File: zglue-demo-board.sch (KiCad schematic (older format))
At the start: 53 parts, among them J1 0473460001, J2 DF13A-2P-1.25H, J3 20021121-00010C4LF, J4 2x20_Header_Female, J5 0473460001, J6 556500488, J7 556500488, J8 WE_686115148922, J9 WE_686115148922, U1 FT232RQ-REEL, U2 NTB0104BQ, U3 NTB0104BQ, U4 NTB0104BQ

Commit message: Added FT4232
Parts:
- removed C4, C6: C_47p_0402, antmicro-footprints:0402-cap, symbol antmicroCapacitors0402:C_47p_0402
- removed C5, C7, C8: C_100n_0402_6V3, antmicro-footprints:0402-cap, symbol antmicroCapacitors0402:C_100n_0402_6V3
- removed D1: TPD2EUSB30DRTR, antmicro-footprints:SOT-3, symbol antmicroTVSDiodes:TPD2EUSB30DRTR
- removed J1: 0473460001, antmicro-footprints:USB_Micro_B_Female_0473460001, symbol antmicroUSBDVIHDMIConnectors:0473460001
- removed R2, R3: R_22R_0402, antmicro-footprints:0402-res, symbol antmicroResistors0402:R_22R_0402
- removed U1: FT232RQ-REEL, antmicro-footprints:QFN-32-1EP_5x5mm, symbol antmicroInterfaceControllers:FT232RQ-REEL
- added C15, C16, C17, C18, C19, C20, C21, C22, C23, C24, C?: C_100n_0402_6V3, antmicro-footprints:0402-cap, symbol antmicroCapacitors0402:C_100n_0402_6V3
- added C25, C26: C_4u7_0402, antmicro-footprints:0402-cap, symbol antmicroCapacitors0402:C_4u7_0402
- added C?: C_10u_0603, antmicro-footprints:0603-cap, symbol antmicroCapacitors0603:C_10u_0603
- added D5: TPD2EUSB30DRTR, antmicro-footprints:SOT-3, symbol antmicroTVSDiodes:TPD2EUSB30DRTR
- added FB1, FB2: BLM18AG601SN1D, antmicro-footprints:0603, symbol antmicroFerriteBeadsandChips:BLM18AG601SN1D
- added J10: 0473460001, antmicro-footprints:USB_Micro_B_Female_0473460001, symbol antmicroUSBDVIHDMIConnectors:0473460001
- added JP1, JP2, JP3: Jumper_3_Open, symbol Jumper:Jumper_3_Open
- added R10, R5: R_2k_0402, antmicro-footprints:0402-res, symbol antmicroResistors0402:R_2k_0402
- added R11, R12, R13, R14, R15, R16, R17, R18, R19, R2, R20, R21, R22, R23, R24, R25, R26, R27, R28, R29, R3, R30, R31, R32, R33, R8: R_0R_0402, antmicro-footprints:0402-res, symbol antmicroResistors0402:R_0R_0402
- added R4, R6, R7: R_10k_0402, antmicro-footprints:0402-res, symbol antmicroResistors0402:R_10k_0402
- added R9: R_12k_0402, antmicro-footprints:0402-res, symbol antmicroResistors0402:R_12k_0402
- added U5: 93LC56CT-IMC, antmicro-footprints:SOIC-8_W3.9mm, symbol antmicroMemory:93LC56CT-IMC
- added U6: FT4232HQ, antmicro-footprints:FT4232HQ, symbol antmicroInterfaceControllers:FT4232HQ
- added U?: LD1117S33CTR, antmicro-footprints:SOT-223, symbol antmicroPMICVoltageRegulatorsLinear:LD1117S33CTR
- added Y1: ASFLMB-12.000MHZ-LC-T, antmicro-footprints:ASFLMB, symbol antmicroOscillators:ASFLMB-12.000MHZ-LC-T
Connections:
- net labels added: 1V8_FTDI, 3V3_FTDI, CTRL_RST_FLASH_SOC_CS, FLASH_CLK, FLASH_CS, FLASH_IO0, FLASH_IO1, FLASH_IO2, FLASH_IO3, PROG_USB_D_N, PROG_USB_D_P, VCCIO, VCCIO1, VCCIO2, VCCIO3, VPHY, VPLL
- net labels removed: PIO1, PIO2, PIO3
- wire segments 281 -> 419
- no-connect marks 23 -> 27
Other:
- note added: "Flash Programming FTDI"
- note added: "Flash Programming USB connector"
- note added: "LDO for FTDI"
- note added: "TODO: no Done signal"
- note removed: "Debug FTDI"
- note removed: "Programming USB connector"
- moved on the sheet: C1, C10, C11, C12, C13, C14, C2, C3, C9, D2, D3, D4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

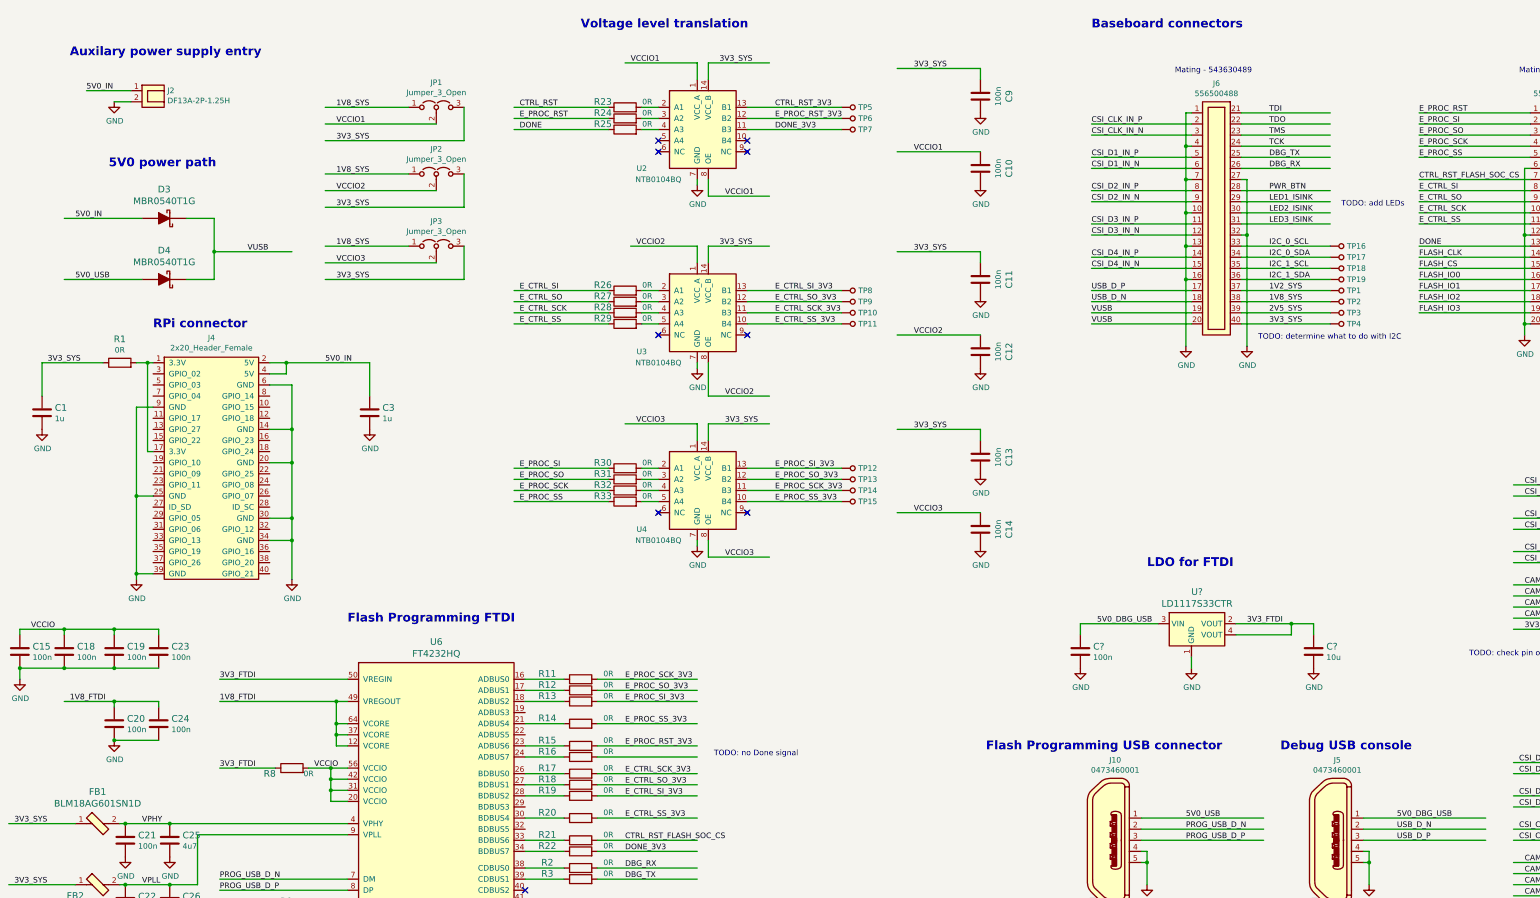
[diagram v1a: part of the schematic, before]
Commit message: Fixed power path
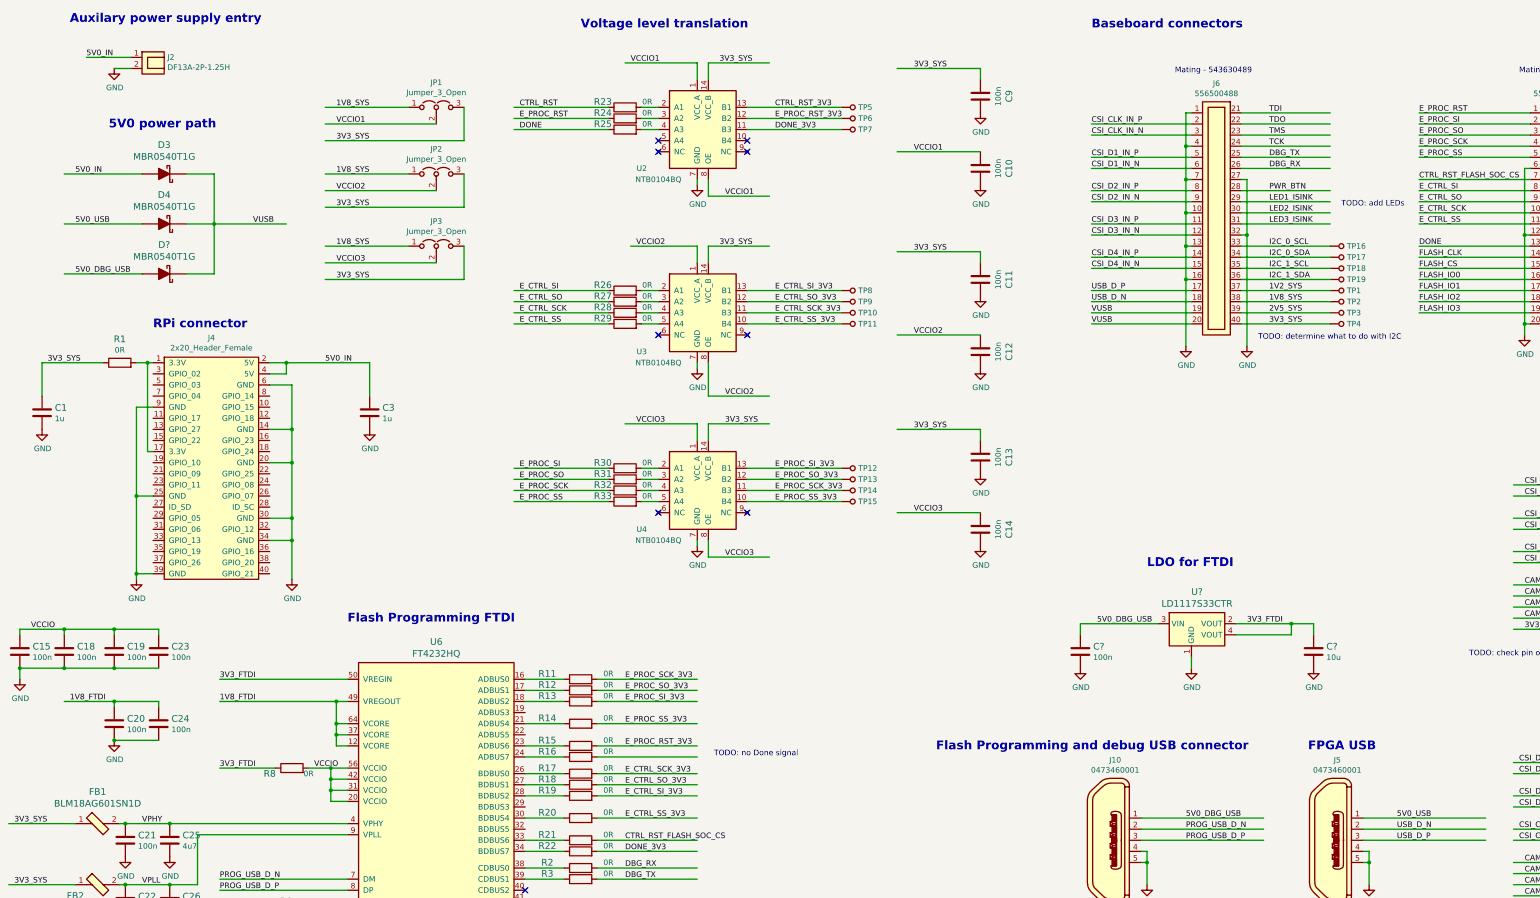
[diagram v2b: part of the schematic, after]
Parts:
- added D?: MBR0540T1G, antmicro-footprints:SOD-123, symbol antmicroDiodesRectifiersSingle:MBR0540T1G
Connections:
- wire segments 419 -> 421
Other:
- note added: "FPGA USB"
- note added: "Flash Programming and debug USB connector"
- note removed: "Debug USB console"
- note removed: "Flash Programming USB connector"
- moved on the sheet: D3, D4, J2
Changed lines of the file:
@@
 L antmicroDF13Connectors:DF13A-2P-1.25H J2
 U 1 1 5DA507A8
-P 1850 1550
-F 0 "J2" H 1978 1701 50  0000 L CNN
-F 1 "DF13A-2P-1.25H" H 1978 1610 50  0000 L CNN
-F 2 "antmicro-footprints:DF13A-2P-1.25H" H 1750 1100 50  0001 C CNN
-F 3 "" H 1850 1500 50  0001 C CNN
-F 4 "DF13A-2P-1.25H" H 1900 1300 50  0001 C CNN "MPN"
-F 5 "Hirose" H 1850 1200 50  0001 C CNN "Manufacturer"
-	1    1850 1550
+P 1850 1250
+F 0 "J2" H 1978 1401 50  0000 L CNN
+F 1 "DF13A-2P-1.25H" H 1978 1310 50  0000 L CNN
+F 2 "antmicro-footprints:DF13A-2P-1.25H" H 1750 800 50  0001 C CNN
+F 3 "" H 1850 1200 50  0001 C CNN
+F 4 "DF13A-2P-1.25H" H 1900 1000 50  0001 C CNN "MPN"
+F 5 "Hirose" H 1850 900 50  0001 C CNN "Manufacturer"
+	1    1850 1250
 	1    0    0    -1
 $EndComp
@@
 3V3_SYS
 Wire Wire Line
-	1650 1400 1250 1400
+	1650 1100 1250 1100
 $Comp
 L power:GND #PWR03
 U 1 1 5DA5701F
-P 1500 1500
-F 0 "#PWR03" H 1500 1250 50  0001 C CNN
-F 1 "GND" H 1505 1327 50  0000 C CNN
-F 2 "" H 1500 1500 50  0001 C CNN
-F 3 "" H 1500 1500 50  0001 C CNN
-	1    1500 1500
-	1    0    0    -1
-$EndComp
-Wire Wire Line
-	1650 1500 1500 1500
+P 1500 1200
+F 0 "#PWR03" H 1500 950 50  0001 C CNN
+F 1 "GND" H 1505 1027 50  0000 C CNN
+F 2 "" H 1500 1200 50  0001 C CNN
+F 3 "" H 1500 1200 50  0001 C CNN
+	1    1500 1200
+	1    0    0    -1
+$EndComp
+Wire Wire Line
+	1650 1200 1500 1200
 $Comp
 L antmicroRectangularConnectorsHeadersMalePins:20021121-00010C4LF J3
@@
 	7700 10500 7550 10500
 Connection ~ 7550 10500
-Text Label 1250 1400 0    50   ~ 0
+Text Label 1250 1100 0    50   ~ 0
 5V0_IN
 $Comp
@@
 	1    0    0    -1
 $EndComp
-Text Notes 1100 1100 0    79   ~ 16
+Text Notes 1100 800  0    79   ~ 16
 Auxilary power supply entry
 Text Notes 1850 3550 0    79   ~ 16
@@
 	1    0    0    -1
 $EndComp
-Text Label 13050 7950 0    50   ~ 0
+Text Label 11150 7950 0    50   ~ 0
 5V0_DBG_USB
 Text Label 3400 3850 0    50   ~ 0
@@
 	1    0    0    -1
 $EndComp
-Text Notes 12000 7350 0    79   ~ 16
-Debug USB console
+Text Notes 12250 7350 0    79   ~ 16
+FPGA USB
 $Comp
 L antmicroTestPoints:TP_SMD1MM TP1
@@
 L antmicroDiodesRectifiersSingle:MBR0540T1G D3
 U 1 1 5DD6DAC1
-P 1950 2550
-F 0 "D3" H 1950 2812 60  0000 C CNN
-F 1 "MBR0540T1G" H 1950 2706 60  0000 C CNN
-F 2 "antmicro-footprints:SOD-123" H 2150 2750 60  0001 L CNN
-F 3 "http://www.onsemi.com/pub/Collateral/MBR0540T1-D.PDF" H 2150 2850 60  0001 L CNN
-F 4 "MBR0540T1G" H 2150 3050 60  0001 L CNN "MPN"
-F 5 "ON Semiconductor" H 2150 3650 60  0001 L CNN "Manufacturer"
-	1    1950 2550
+P 1950 2150
+F 0 "D3" H 1950 2412 60  0000 C CNN
+F 1 "MBR0540T1G" H 1950 2306 60  0000 C CNN
+F 2 "antmicro-footprints:SOD-123" H 2150 2350 60  0001 L CNN
+F 3 "http://www.onsemi.com/pub/Collateral/MBR0540T1-D.PDF" H 2150 2450 60  0001 L CNN
+F 4 "MBR0540T1G" H 2150 2650 60  0001 L CNN "MPN"
+F 5 "ON Semiconductor" H 2150 3250 60  0001 L CNN "Manufacturer"
+	1    1950 2150
 	1    0    0    -1
 $EndComp
@@
 L antmicroDiodesRectifiersSingle:MBR0540T1G D4
 U 1 1 5DD6DCA3
-P 1950 3100
-F 0 "D4" H 1950 3362 60  0000 C CNN
-F 1 "MBR0540T1G" H 1950 3256 60  0000 C CNN
-F 2 "antmicro-footprints:SOD-123" H 2150 3300 60  0001 L CNN
-F 3 "http://www.onsemi.com/pub/Collateral/MBR0540T1-D.PDF" H 2150 3400 60  0001 L CNN
-F 4 "MBR0540T1G" H 2150 3600 60  0001 L CNN "MPN"
-F 5 "ON Semiconductor" H 2150 4200 60  0001 L CNN "Manufacturer"
-	1    1950 3100
-	1    0    0    -1
-$EndComp
-Wire Wire Line
-	1750 2550 1050 2550
-Wire Wire Line
-	1750 3100 1050 3100
-Wire Wire Line
-	2150 2550 2400 2550
-Wire Wire Line
-	2400 2550 2400 2850
-Wire Wire Line
-	2400 2850 3100 2850
-Wire Wire Line
-	2400 2850 2400 3100
-Wire Wire Line
-	2400 3100 2150 3100
-Connection ~ 2400 2850
-Text Label 2700 2850 0    50   ~ 0
+P 1950 2600
+F 0 "D4" H 1950 2862 60  0000 C CNN
+F 1 "MBR0540T1G" H 1950 2756 60  0000 C CNN
+F 2 "antmicro-footprints:SOD-123" H 2150 2800 60  0001 L CNN
+F 3 "http://www.onsemi.com/pub/Collateral/MBR0540T1-D.PDF" H 2150 2900 60  0001 L CNN
+F 4 "MBR0540T1G" H 2150 3100 60  0001 L CNN "MPN"
+F 5 "ON Semiconductor" H 2150 3700 60  0001 L CNN "Manufacturer"
+	1    1950 2600
+	1    0    0    -1
+$EndComp
+Wire Wire Line
+	1750 2150 1050 2150
+Wire Wire Line
+	1750 2600 1050 2600
+Wire Wire Line
+	2150 2150 2400 2150
+Wire Wire Line
+	2400 2600 2150 2600
+Text Label 2750 2600 0    50   ~ 0
 VUSB
-Text Label 1150 2550 0    50   ~ 0
+Text Label 1150 2150 0    50   ~ 0
 5V0_IN
-Text Label 1150 3100 0    50   ~ 0
+Text Label 1150 2600 0    50   ~ 0
 5V0_USB
-Text Notes 1450 2100 0    79   ~ 16
+Text Notes 1450 1750 0    79   ~ 16
 5V0 power path
 $Comp
@@
 	1    0    0    -1
 $EndComp
-Text Label 11150 7950 0    50   ~ 0
+Text Label 13050 7950 0    50   ~ 0
 5V0_USB
 Text Label 11150 8150 0    50   ~ 0
@@
 Text Label 11150 8050 0    50   ~ 0
 PROG_USB_D_N
-Text Notes 9350 7350 0    79   ~ 16
-Flash Programming USB connector
+Text Notes 8900 7350 0    79   ~ 16
+Flash Programming and debug USB connector
 $Comp
 L antmicroTVSDiodes:TPD2EUSB30DRTR D5
@@
 	12300 6200 12300 6300
 Connection ~ 12100 6200
+$Comp
+L antmicroDiodesRectifiersSingle:MBR0540T1G D?
+U 1 1 5DB10412
+P 1950 3050
+F 0 "D?" H 1950 3312 60  0000 C CNN
+F 1 "MBR0540T1G" H 1950 3206 60  0000 C CNN
+F 2 "antmicro-footprints:SOD-123" H 2150 3250 60  0001 L CNN
+F 3 "http://www.onsemi.com/pub/Collateral/MBR0540T1-D.PDF" H 2150 3350 60  0001 L CNN
+F 4 "MBR0540T1G" H 2150 3550 60  0001 L CNN "MPN"
+F 5 "ON Semiconductor" H 2150 4150 60  0001 L CNN "Manufacturer"
+	1    1950 3050
+	1    0    0    -1
+$EndComp
+Wire Wire Line
+	2400 2150 2400 2600
+Wire Wire Line
+	2400 2600 2400 3050
+Wire Wire Line
+	2400 3050 2150 3050
+Connection ~ 2400 2600
+Wire Wire Line
+	2400 2600 3050 2600
+Wire Wire Line
+	1750 3050 1050 3050
+Text Label 1150 3050 0    50   ~ 0
+5V0_DBG_USB
 $EndSCHEMATC

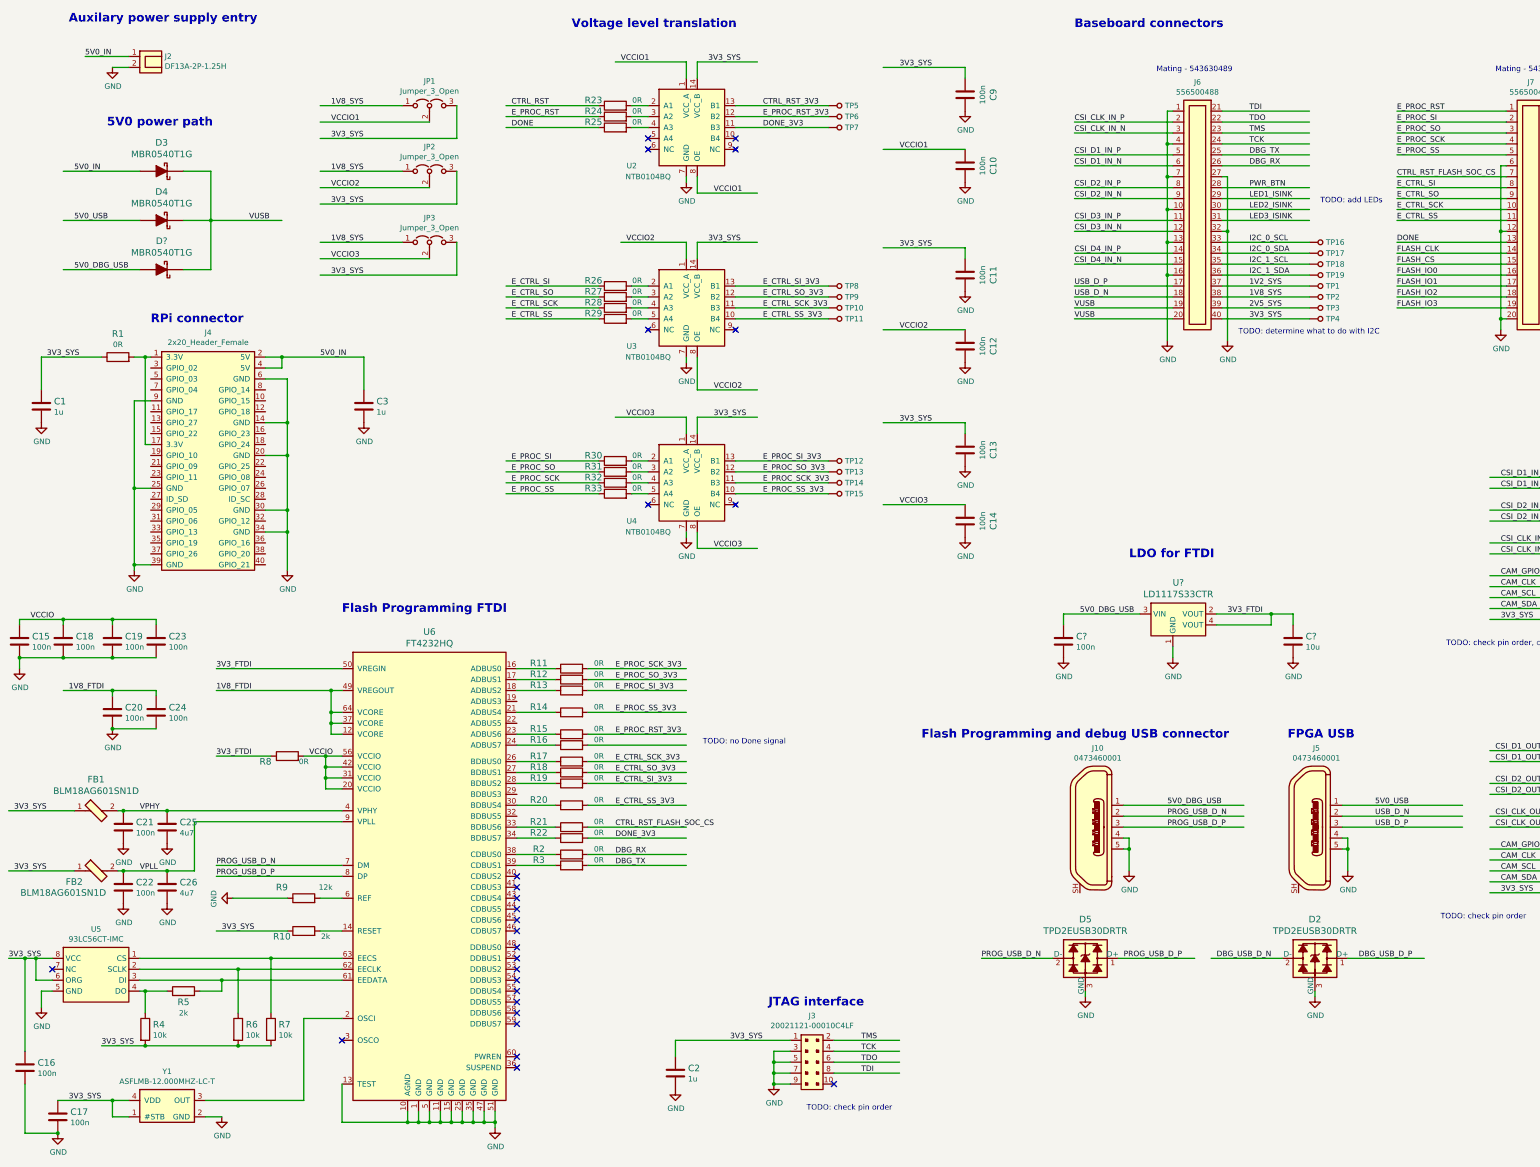
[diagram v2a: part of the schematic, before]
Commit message: Unified 3V3 voltage rails
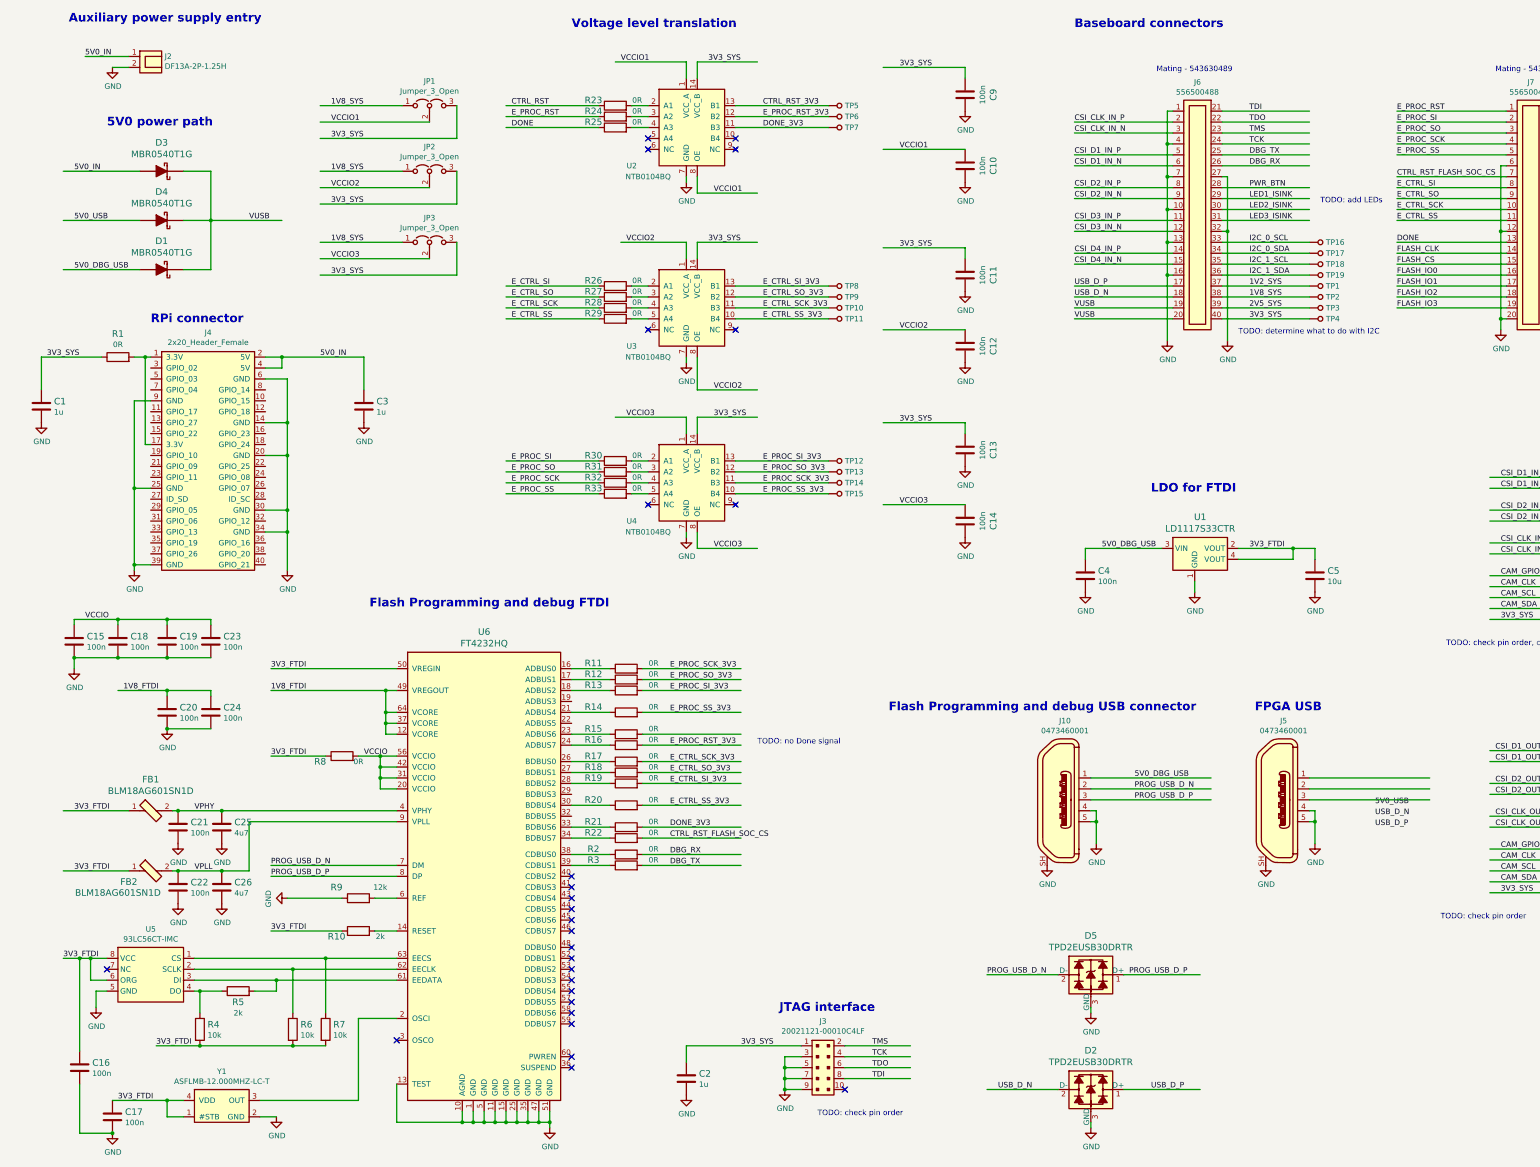
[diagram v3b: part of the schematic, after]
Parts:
- gave numbers to parts that had none: 4
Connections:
- net labels removed: DBG_USB_D_N, DBG_USB_D_P
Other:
- note added: "Auxiliary power supply entry"
- note added: "Flash Programming and debug FTDI"
- note removed: "Auxilary power supply entry"
- note removed: "Flash Programming FTDI"
- moved on the sheet: C15, C16, C17, C18, C19, C2, C20, C21, C22, C23, C24, C25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
